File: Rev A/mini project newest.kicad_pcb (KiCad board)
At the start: 2 copper layers, 82.5 x 63.5 mm, 26 parts, among them J1 Conn_01x02, Q1 Q_NMOS_SGD, U1 LM555, U2 LM555

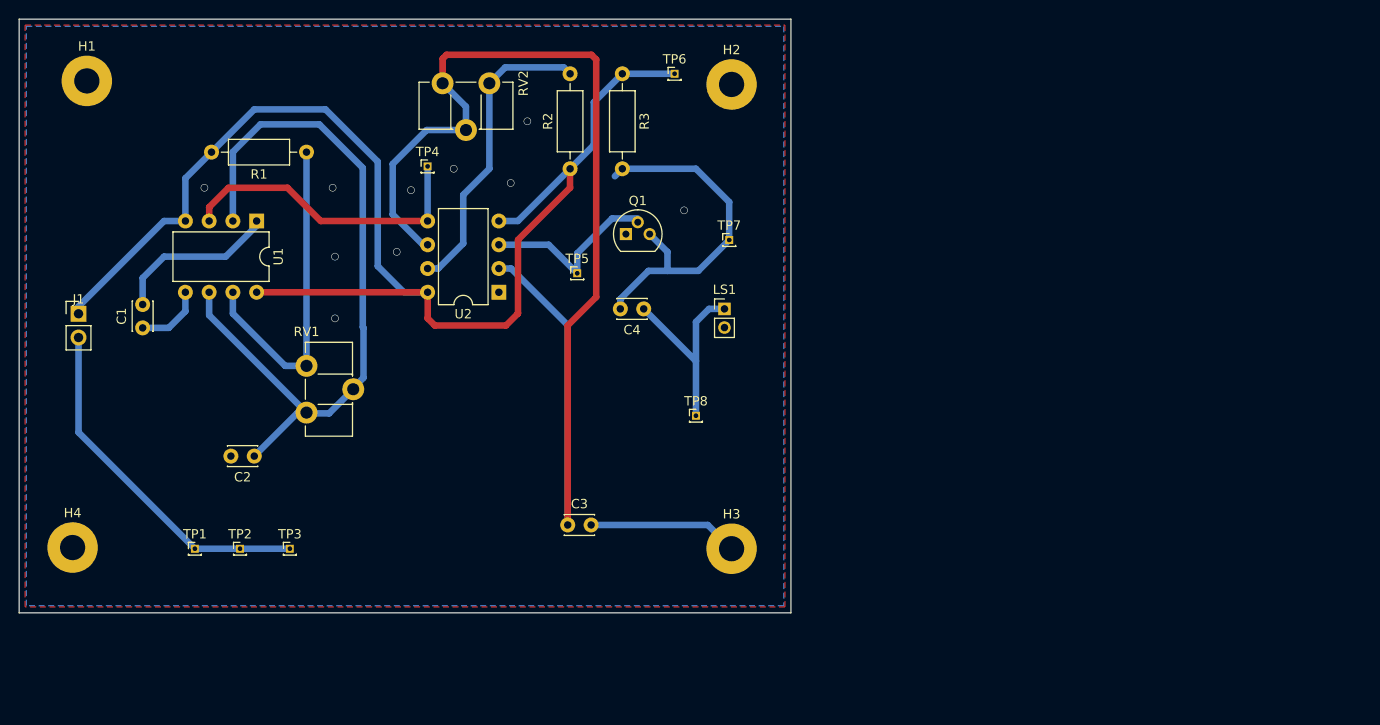
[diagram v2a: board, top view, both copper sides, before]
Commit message: shortened some traces, theres a problem with the ground pin for power
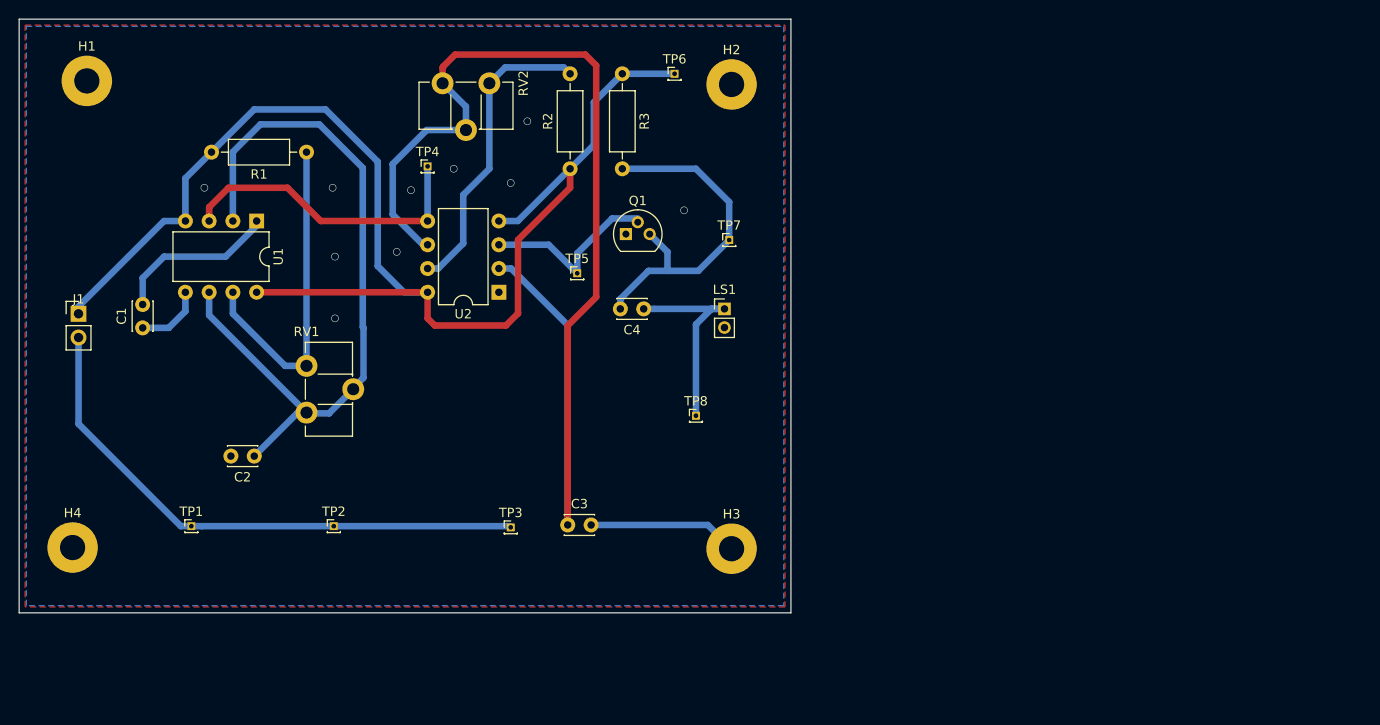
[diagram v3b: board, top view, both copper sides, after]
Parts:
- moved TP3 23.7 mm to (97.0, 111.5)
- moved TP2 10.3 mm to (78.1, 111.4)
- moved TP1 2.44 mm to (62.9, 111.4)
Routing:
- net GND: track 37.9 -> 60.0 mm
- net Net-(C4-Pad2): track 37.9 -> 36.8 mm
- net Net-(C3-Pad1): track 127.6 -> 126.7 mm
- net Net-(C4-Pad1): track 21.6 -> 22.1 mm
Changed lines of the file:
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@@
     (thickness 1.6)
     (drawings 4)
-    (tracks 122)
+    (tracks 126)
     (zones 0)
     (modules 26)
@@
   )
   (module Connector_PinHeader_1.00mm:PinHeader_1x01_P1.00mm_Vertical (layer F.Cu)
-    (at 73.406 113.792)
+    (at 97.028 111.506)
     (descr "Through hole straight pin header, 1x01, 1.00mm pitch, single row")
     (tags "Through hole pin header THT 1x01 1.00mm single row")
@@
   )
   (module Connector_PinHeader_1.00mm:PinHeader_1x01_P1.00mm_Vertical (layer F.Cu)
-    (at 68.072 113.792)
+    (at 78.105 111.379)
     (descr "Through hole straight pin header, 1x01, 1.00mm pitch, single row")
     (tags "Through hole pin header THT 1x01 1.00mm single row")
@@
   )
   (module Connector_PinHeader_1.00mm:PinHeader_1x01_P1.00mm_Vertical (layer F.Cu)
-    (at 63.246 113.792)
+    (at 62.865 111.379)
     (descr "Through hole straight pin header, 1x01, 1.00mm pitch, single row")
     (tags "Through hole pin header THT 1x01 1.00mm single row")
@@
   (via (at 115.57 77.597) (size 0.8) (drill 0.70104) (layers F.Cu B.Cu) (net 0))
   (segment (start 105.33 111.045) (end 105.41 111.125) (width 0.25) (layer B.Cu) (net 1))
-  (segment (start 118.11 111.252) (end 120.65 113.792) (width 0.70104) (layer B.Cu) (net 1))
-  (segment (start 105.624 111.252) (end 118.11 111.252) (width 0.70104) (layer B.Cu) (net 1))
   (segment (start 57.658 87.67) (end 57.658 84.836) (width 0.70104) (layer B.Cu) (net 1))
   (segment (start 57.658 84.836) (end 59.944 82.55) (width 0.70104) (layer B.Cu) (net 1))
@@
   (via (at 84.836 82.042) (size 0.8) (drill 0.70104) (layers F.Cu B.Cu) (net 1))
   (via (at 64.262 75.184) (size 0.8) (drill 0.70104) (layers F.Cu B.Cu) (net 1))
+  (segment (start 118.11 111.252) (end 120.65 113.792) (width 0.70104) (layer B.Cu) (net 1))
+  (segment (start 105.624 111.252) (end 118.11 111.252) (width 0.70104) (layer B.Cu) (net 1))
   (segment (start 57.658 90.17) (end 60.452 90.17) (width 0.70104) (layer B.Cu) (net 2))
   (segment (start 62.23 88.392) (end 62.23 86.36) (width 0.70104) (layer B.Cu) (net 2))
@@
   (segment (start 103.124 111.252) (end 103.124 89.876574) (width 0.70104) (layer B.Cu) (net 4))
   (segment (start 103.124 89.916) (end 103.124 111.252) (width 0.70104) (layer F.Cu) (net 4))
-  (segment (start 89.742 61.388) (end 90.17 60.96) (width 0.70104) (layer F.Cu) (net 4))
-  (segment (start 89.742 64.008) (end 89.742 61.388) (width 0.70104) (layer F.Cu) (net 4))
-  (segment (start 90.17 60.96) (end 105.664 60.96) (width 0.70104) (layer F.Cu) (net 4))
-  (segment (start 105.664 60.96) (end 106.172 61.468) (width 0.70104) (layer F.Cu) (net 4))
-  (segment (start 106.172 61.468) (end 106.172 86.868) (width 0.70104) (layer F.Cu) (net 4))
   (segment (start 106.172 86.868) (end 103.124 89.916) (width 0.70104) (layer F.Cu) (net 4))
-  (segment (start 116.84 93.726) (end 111.252 88.138) (width 0.70104) (layer B.Cu) (net 5))
-  (segment (start 116.84 99.568) (end 116.84 93.726) (width 0.70104) (layer B.Cu) (net 5))
-  (segment (start 118.237 88.138) (end 119.888 88.138) (width 0.70104) (layer B.Cu) (net 5))
-  (segment (start 116.84 93.726) (end 116.84 89.535) (width 0.70104) (layer B.Cu) (net 5))
-  (segment (start 116.84 89.535) (end 118.237 88.138) (width 0.70104) (layer B.Cu) (net 5))
+  (segment (start 89.742 62.353371) (end 89.789 62.306371) (width 0.70104) (layer F.Cu) (net 4))
+  (segment (start 89.742 64.008) (end 89.742 62.353371) (width 0.70104) (layer F.Cu) (net 4))
+  (segment (start 89.789 62.306371) (end 89.789 62.23) (width 0.70104) (layer F.Cu) (net 4))
+  (segment (start 91.076681 60.942319) (end 105.011319 60.942319) (width 0.70104) (layer F.Cu) (net 4))
+  (segment (start 89.789 62.23) (end 91.076681 60.942319) (width 0.70104) (layer F.Cu) (net 4))
+  (segment (start 106.172 62.103) (end 106.172 86.868) (width 0.70104) (layer F.Cu) (net 4))
+  (segment (start 105.011319 60.942319) (end 106.172 62.103) (width 0.70104) (layer F.Cu) (net 4))
+  (segment (start 112.38337 88.138) (end 119.888 88.138) (width 0.70104) (layer B.Cu) (net 5))
+  (segment (start 111.252 88.138) (end 112.38337 88.138) (width 0.70104) (layer B.Cu) (net 5))
+  (segment (start 118.51196 88.138) (end 119.888 88.138) (width 0.70104) (layer B.Cu) (net 5))
+  (segment (start 116.84 99.568) (end 116.84 89.80996) (width 0.70104) (layer B.Cu) (net 5))
+  (segment (start 116.84 89.80996) (end 118.51196 88.138) (width 0.70104) (layer B.Cu) (net 5))
   (segment (start 120.396 80.772) (end 120.396 76.708) (width 0.70104) (layer B.Cu) (net 6))
   (segment (start 116.84 73.152) (end 108.966 73.152) (width 0.70104) (layer B.Cu) (net 6))
@@
   (segment (start 108.752 87.082) (end 111.76 84.074) (width 0.70104) (layer B.Cu) (net 6))
   (segment (start 117.094 84.074) (end 120.396 80.772) (width 0.70104) (layer B.Cu) (net 6))
-  (segment (start 108.966 73.152) (end 108.166001 73.951999) (width 0.70104) (layer B.Cu) (net 6))
   (segment (start 113.792 82.042) (end 112.022765 80.272765) (width 0.70104) (layer B.Cu) (net 6))
   (segment (start 113.792 84.074) (end 113.792 82.042) (width 0.70104) (layer B.Cu) (net 6))
@@
   (segment (start 96.52 89.916) (end 97.807681 88.628319) (width 0.70104) (layer F.Cu) (net 7))
   (segment (start 97.807681 88.628319) (end 97.807681 80.754319) (width 0.70104) (layer F.Cu) (net 7))
-  (segment (start 101.092 81.28) (end 104.14 84.328) (width 0.70104) (layer B.Cu) (net 12))
-  (segment (start 95.758 81.28) (end 101.092 81.28) (width 0.70104) (layer B.Cu) (net 12))
   (segment (start 67.31 86.36) (end 67.31 88.646) (width 0.70104) (layer B.Cu) (net 8))
   (segment (start 72.898 94.234) (end 75.184 94.234) (width 0.70104) (layer B.Cu) (net 8))
@@
   (segment (start 94.742 73.152) (end 94.742 64.008) (width 0.70104) (layer B.Cu) (net 9))
   (segment (start 91.948 75.946) (end 94.742 73.152) (width 0.70104) (layer B.Cu) (net 9))
-  (segment (start 63.246 113.792) (end 68.072 113.792) (width 0.70104) (layer B.Cu) (net 10))
-  (segment (start 68.072 113.792) (end 73.406 113.792) (width 0.70104) (layer B.Cu) (net 10))
-  (segment (start 50.8 101.346) (end 63.246 113.792) (width 0.70104) (layer B.Cu) (net 10))
-  (segment (start 50.8 91.202) (end 50.8 101.346) (width 0.70104) (layer B.Cu) (net 10))
+  (segment (start 61.73896 111.379) (end 50.8 100.44004) (width 0.70104) (layer B.Cu) (net 10))
+  (segment (start 62.865 111.379) (end 61.73896 111.379) (width 0.70104) (layer B.Cu) (net 10))
+  (segment (start 50.8 100.44004) (end 50.8 91.202) (width 0.70104) (layer B.Cu) (net 10))
+  (segment (start 63.99104 111.379) (end 78.105 111.379) (width 0.70104) (layer B.Cu) (net 10))
+  (segment (start 62.865 111.379) (end 63.99104 111.379) (width 0.70104) (layer B.Cu) (net 10))
+  (segment (start 96.901 111.379) (end 97.028 111.506) (width 0.70104) (layer B.Cu) (net 10))
+  (segment (start 78.105 111.379) (end 96.901 111.379) (width 0.70104) (layer B.Cu) (net 10))
   (segment (start 88.138 78.74) (end 88.138 72.898) (width 0.70104) (layer B.Cu) (net 11))
   (segment (start 64.77 77.265833) (end 64.77 78.74) (width 0.70104) (layer F.Cu) (net 11))
@@
   (segment (start 73.152 75.184) (end 66.851833 75.184) (width 0.70104) (layer F.Cu) (net 11))
   (segment (start 88.138 78.74) (end 76.708 78.74) (width 0.70104) (layer F.Cu) (net 11))
+  (segment (start 101.092 81.28) (end 104.14 84.328) (width 0.70104) (layer B.Cu) (net 12))
+  (segment (start 95.758 81.28) (end 101.092 81.28) (width 0.70104) (layer B.Cu) (net 12))
   (segment (start 107.877671 78.462839) (end 110.617 78.462839) (width 0.70104) (layer B.Cu) (net 12))
   (segment (start 104.14 84.328) (end 104.14 82.20051) (width 0.70104) (layer B.Cu) (net 12))
   (segment (start 104.14 82.20051) (end 107.877671 78.462839) (width 0.70104) (layer B.Cu) (net 12))
+  (zone (net 1) (net_name Earth) (layer B.Cu) (hatch edge 0.508)
+    (connect_pads (clearance 0.508))
+    (min_thickness 0.254)
+    (fill yes (arc_segments 32) (thermal_gap 0.508) (thermal_bridge_width 0.508))
+    (polygon
+      (pts
+        (xy 126.238 119.888) (xy 45.212 119.888) (xy 45.212 57.912) (xy 126.238 57.912)
+      )
+    )
+  )
   (zone (net 1) (net_name Earth) (layer F.Cu) (hatch edge 0.508)
     (connect_pads (clearance 0.508))
@@
       )
     )
-  )
-  (zone (net 1) (net_name Earth) (layer B.Cu) (hatch edge 0.508)
-    (connect_pads (clearance 0.508))
-    (min_thickness 0.254)
-    (fill yes (arc_segments 32) (thermal_gap 0.508) (thermal_bridge_width 0.508))
-    (polygon
-      (pts
-        (xy 126.238 119.888) (xy 45.212 119.888) (xy 45.212 57.912) (xy 126.238 57.912)
-      )
-    )

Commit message: Fixed traces not grounding properly, fixed pad too close to pad bugs, finished silkscreen, changed mounting hole sizes, repositioned TPs
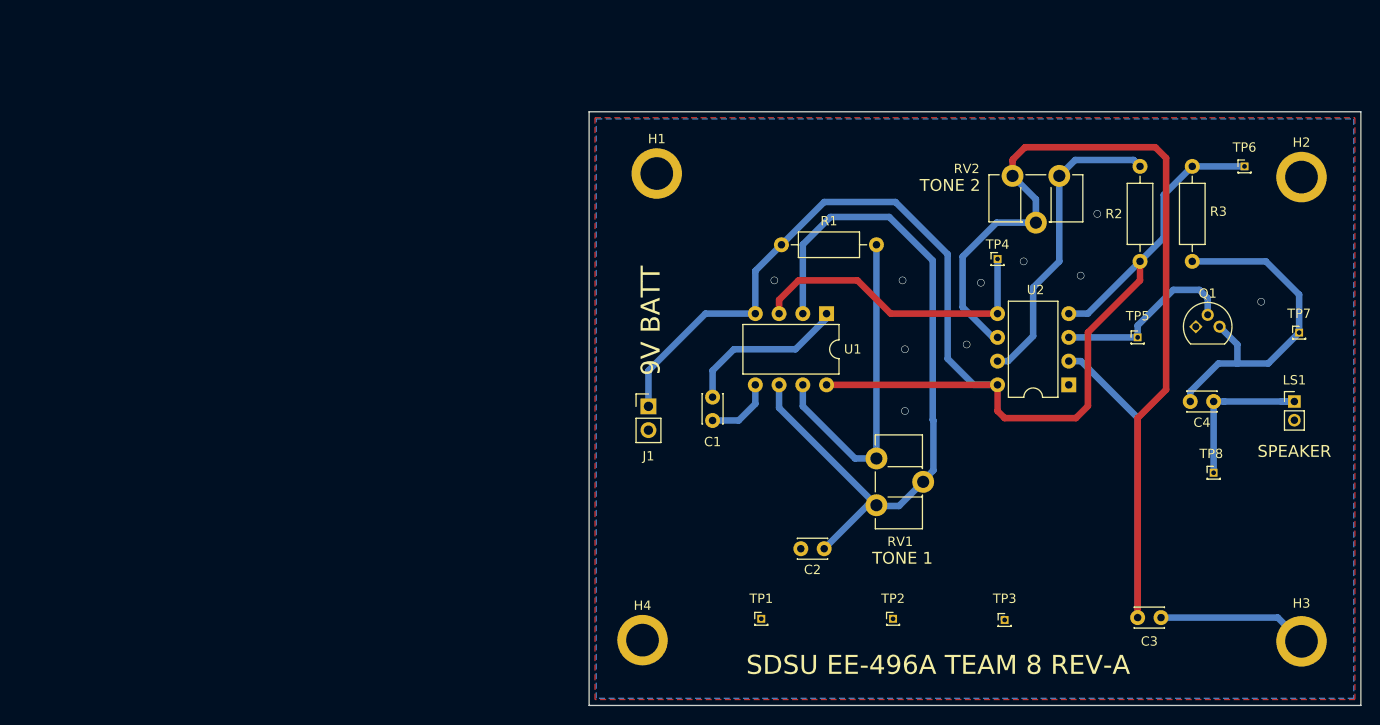
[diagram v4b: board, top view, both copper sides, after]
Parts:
- moved C2 61.8 mm to (130.6, 113.8)
- moved C3 61.8 mm to (164.1, 121.2)
- moved H2 61.8 mm to (181.6, 74.0)
- moved H3 61.8 mm to (181.6, 123.7)
- moved J1 61.8 mm to (111.8, 98.6)
- moved LS1 61.8 mm to (180.8, 98.0)
- moved R1 61.8 mm to (136.1, 81.3)
- moved RV1 61.8 mm to (136.1, 104.1)
- moved TP4 61.8 mm to (149.1, 82.8)
- moved TP6 61.8 mm to (175.5, 72.9)
- moved U1 61.8 mm to (130.8, 88.6)
- moved H1 61.8 mm to (112.6, 73.7)
- moved H4 61.8 mm to (111.1, 123.6)
- moved TP1 61.8 mm to (123.8, 121.3)
- moved C1 61.8 mm to (118.6, 100.1)
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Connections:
- J1 pad 2: GND -> Earth
- TP1 pad 1: GND -> Earth
- TP2 pad 1: GND -> Earth
- TP3 pad 1: GND -> Earth
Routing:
- net GND: track 60.0 -> 0.00 mm
- net Net-(C4-Pad1): track 22.1 -> 17.6 mm
- net +9V: track 141.6 -> 143.3 mm
- net Net-(Q1-Pad2): track 19.8 -> 19.2 mm
- net Earth: track 34.0 -> 34.2 mm, vias 9 -> 10
- net (no net): vias 1 -> 0
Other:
- board size 82.5 x 63.5 mm -> 82.6 x 63.5 mm
- board text added: "9V BATT"
- board text added: "SDSU EE-496A TEAM 8 REV-A"
- board text added: "SPEAKER"
- board text added: "TONE 1"
- board text added: "TONE 2"
